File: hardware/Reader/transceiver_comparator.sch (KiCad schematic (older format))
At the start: 12 parts, among them IC7 LM339N_NOPB

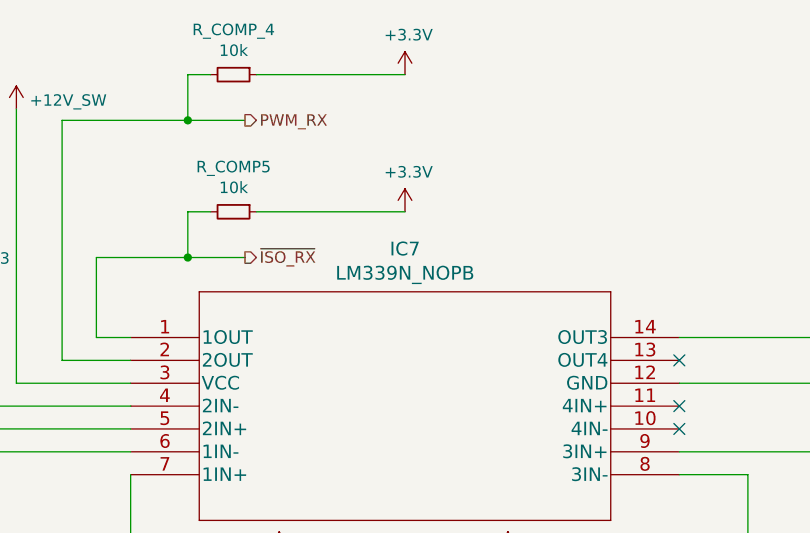
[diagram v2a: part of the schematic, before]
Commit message: Added ESD Protection. Fixed minor bugs on schematic. Attempted placement of components
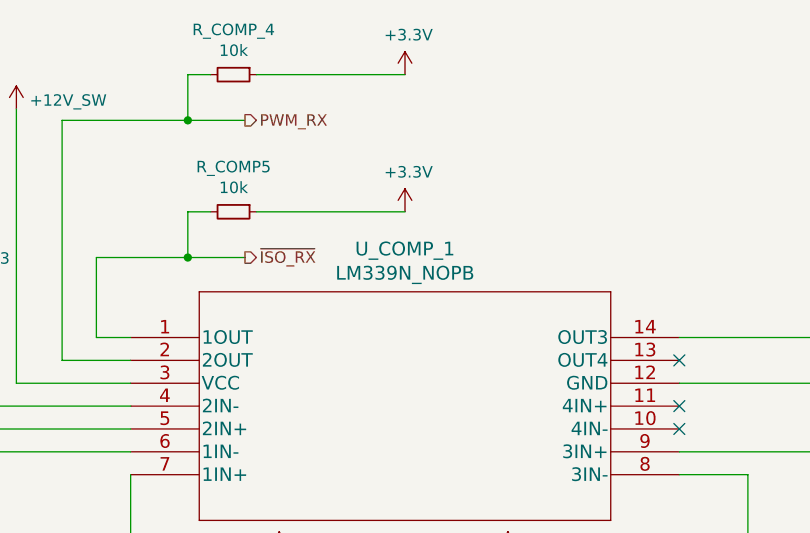
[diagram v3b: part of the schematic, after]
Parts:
- renumbered IC7 to U_COMP_1
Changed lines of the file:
@@
 $Descr USLetter 11000 8500
 encoding utf-8
-Sheet 13 18
+Sheet 8 19
 Title "CANnect Reader | Comparative Transceiver"
-Date "2020-10-20"
-Rev "0.0.01"
+Date "2020-10-25"
+Rev "0.0.03"
 Comp "CANtech"
 Comment1 "Created by Choong Jin Ng | jin8383@gmail.com"
@@
 P 4600 2200
 AR Path="/5F95F80B/5FA83833/5FB4E413" Ref="U?"  Part="1"
-AR Path="/5F95F80B/5FB4CA84/5FB4E413" Ref="IC7"  Part="1"
-F 0 "IC7" H 5800 2587 60  0000 C CNN
+AR Path="/5F95F80B/5FB4CA84/5FB4E413" Ref="U_COMP_1"  Part="1"
+F 0 "U_COMP_1" H 5800 2587 60  0000 C CNN
 F 1 "LM339N_NOPB" H 5800 2481 60  0000 C CNN
 F 2 "footprints:LM339N&slash_NOPB" H 5800 2440 60  0001 C CNN

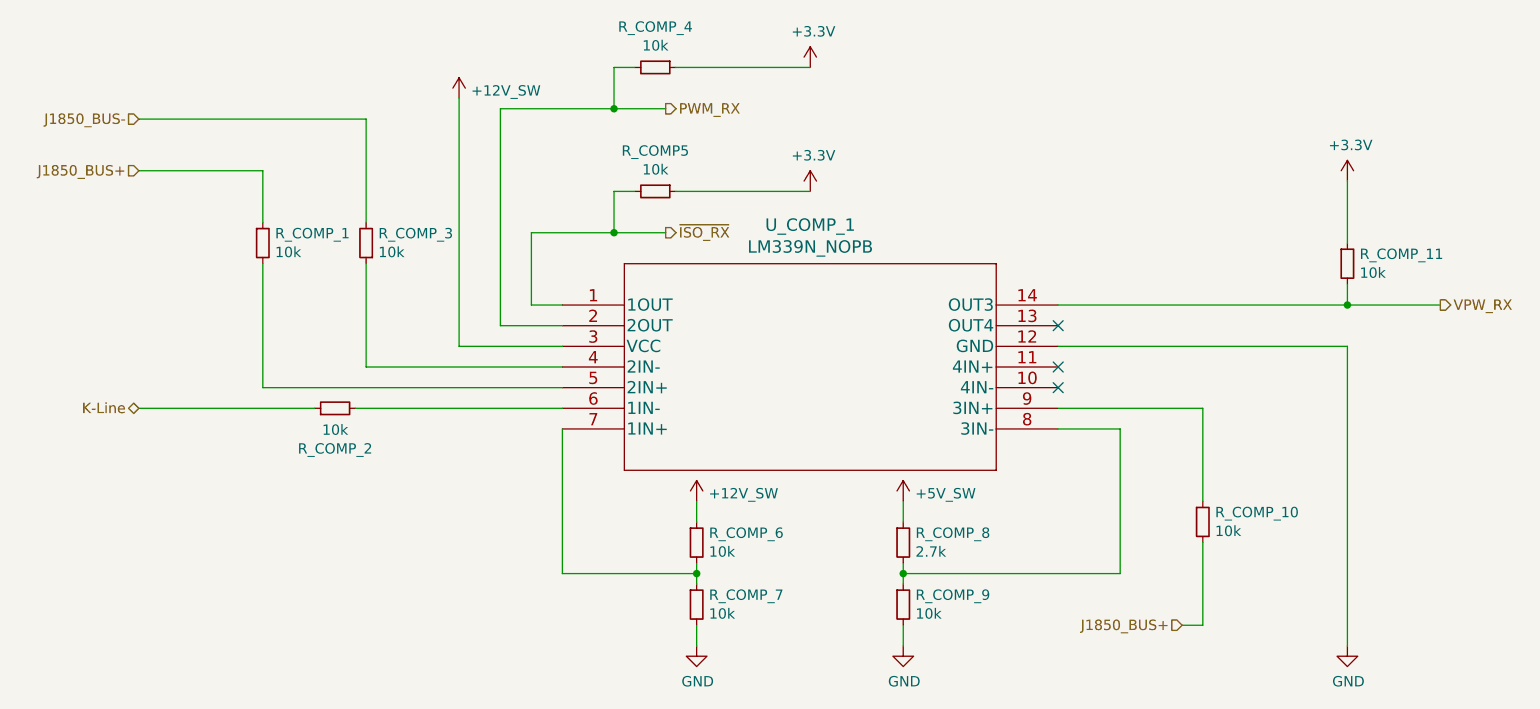
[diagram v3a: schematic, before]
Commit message: Fixed bugs on the reader schematic. Exported Schematic Electrical report
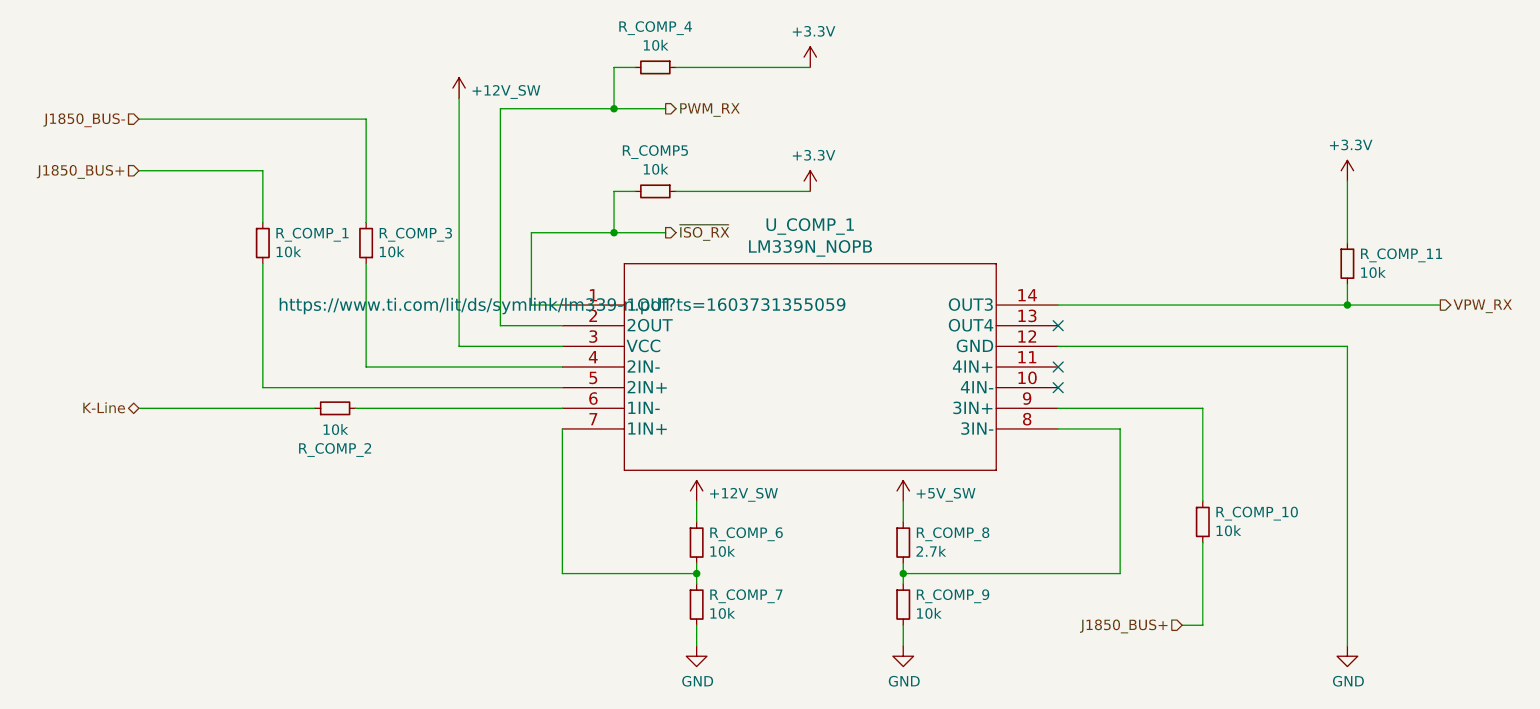
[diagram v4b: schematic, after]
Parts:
- R_COMP5, R_COMP_1, R_COMP_10, R_COMP_11, R_COMP_2, R_COMP_3, R_COMP_4, R_COMP_6, R_COMP_7, R_COMP_9: Manufacturer (none) -> Yageo; Vendor (none) -> DigiKey Canada; digikeypn (none) -> YAG2321CT-ND
- R_COMP_8: Manufacturer (none) -> Vishay Dale; Vendor (none) -> DigiKey Canada; digikeypn (none) -> 541-5328-1-ND
- U_COMP_1: Manufacturer (none) -> Texas Instruments; Part Name (none) -> LM339N_NOPB; Vendor (none) -> DigiKey Canada; digikeypn (none) -> 296-39010-5-ND
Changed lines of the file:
@@
 F 3 "https://www.yageo.com/upload/media/product/productsearch/datasheet/rchip/PYu-RT_1-to-0.01_RoHS_L_12.pdf" H 5250 3350 50  0001 C CNN
 F 4 "RT0603FRE0710KL" H 5250 3350 50  0001 C CNN "Part Name"
+F 5 "DigiKey Canada" H 5250 3350 50  0001 C CNN "Vendor"
+F 6 "YAG2321CT-ND" H 5250 3350 50  0001 C CNN "digikeypn"
+F 7 "Yageo" H 5250 3350 50  0001 C CNN "Manufacturer"
 	1    5250 3350
 	1    0    0    -1
@@
 F 3 "https://www.yageo.com/upload/media/product/productsearch/datasheet/rchip/PYu-RT_1-to-0.01_RoHS_L_12.pdf" H 5250 3650 50  0001 C CNN
 F 4 "RT0603FRE0710KL" H 5250 3650 50  0001 C CNN "Part Name"
+F 5 "DigiKey Canada" H 5250 3650 50  0001 C CNN "Vendor"
+F 6 "YAG2321CT-ND" H 5250 3650 50  0001 C CNN "digikeypn"
+F 7 "Yageo" H 5250 3650 50  0001 C CNN "Manufacturer"
 	1    5250 3650
 	1    0    0    -1
@@
 F 3 "https://www.yageo.com/upload/media/product/productsearch/datasheet/rchip/PYu-RT_1-to-0.01_RoHS_L_12.pdf" H 5050 1650 50  0001 C CNN
 F 4 "RT0603FRE0710KL" H 5050 1650 50  0001 C CNN "Part Name"
+F 5 "DigiKey Canada" H 5050 1650 50  0001 C CNN "Vendor"
+F 6 "YAG2321CT-ND" H 5050 1650 50  0001 C CNN "digikeypn"
+F 7 "Yageo" H 5050 1650 50  0001 C CNN "Manufacturer"
 	1    5050 1650
 	0    1    1    0
@@
 F 3 "https://www.yageo.com/upload/media/product/productsearch/datasheet/rchip/PYu-RT_1-to-0.01_RoHS_L_12.pdf" H 3650 1900 50  0001 C CNN
 F 4 "RT0603FRE0710KL" H 3650 1900 50  0001 C CNN "Part Name"
+F 5 "DigiKey Canada" H 3650 1900 50  0001 C CNN "Vendor"
+F 6 "YAG2321CT-ND" H 3650 1900 50  0001 C CNN "digikeypn"
+F 7 "Yageo" H 3650 1900 50  0001 C CNN "Manufacturer"
 	1    3650 1900
 	-1   0    0    1
@@
 F 3 "https://www.yageo.com/upload/media/product/productsearch/datasheet/rchip/PYu-RT_1-to-0.01_RoHS_L_12.pdf" H 3150 1900 50  0001 C CNN
 F 4 "RT0603FRE0710KL" H 3150 1900 50  0001 C CNN "Part Name"
+F 5 "DigiKey Canada" H 3150 1900 50  0001 C CNN "Vendor"
+F 6 "YAG2321CT-ND" H 3150 1900 50  0001 C CNN "digikeypn"
+F 7 "Yageo" H 3150 1900 50  0001 C CNN "Manufacturer"
 	1    3150 1900
 	1    0    0    -1
@@
 F 3 "https://www.yageo.com/upload/media/product/productsearch/datasheet/rchip/PYu-RT_1-to-0.01_RoHS_L_12.pdf" H 7700 3250 50  0001 C CNN
 F 4 "RT0603FRE0710KL" H 7700 3250 50  0001 C CNN "Part Name"
+F 5 "DigiKey Canada" H 7700 3250 50  0001 C CNN "Vendor"
+F 6 "YAG2321CT-ND" H 7700 3250 50  0001 C CNN "digikeypn"
+F 7 "Yageo" H 7700 3250 50  0001 C CNN "Manufacturer"
 	1    7700 3250
 	1    0    0    -1
@@
 F 3 "https://www.vishay.com/docs/28773/crcwce3.pdf" H 6250 3350 50  0001 C CNN
 F 4 "CRCW06032K70FKEAC" H 6250 3350 50  0001 C CNN "Part Name"
+F 5 "DigiKey Canada" H 6250 3350 50  0001 C CNN "Vendor"
+F 6 "Vishay Dale" H 6250 3350 50  0001 C CNN "Manufacturer"
+F 7 "541-5328-1-ND" H 6250 3350 50  0001 C CNN "digikeypn"
 	1    6250 3350
 	1    0    0    -1
@@
 F 3 "https://www.yageo.com/upload/media/product/productsearch/datasheet/rchip/PYu-RT_1-to-0.01_RoHS_L_12.pdf" H 6250 3650 50  0001 C CNN
 F 4 "RT0603FRE0710KL" H 6250 3650 50  0001 C CNN "Part Name"
+F 5 "DigiKey Canada" H 6250 3650 50  0001 C CNN "Vendor"
+F 6 "YAG2321CT-ND" H 6250 3650 50  0001 C CNN "digikeypn"
+F 7 "Yageo" H 6250 3650 50  0001 C CNN "Manufacturer"
 	1    6250 3650
 	1    0    0    -1
@@
 F 1 "LM339N_NOPB" H 5800 2481 60  0000 C CNN
 F 2 "footprints:LM339N&slash_NOPB" H 5800 2440 60  0001 C CNN
-F 3 "" H 4600 2200 60  0000 C CNN
+F 3 "https://www.ti.com/lit/ds/symlink/lm339-n.pdf?ts=1603731355059" H 4600 2200 60  0000 C CNN
+F 4 "LM339N_NOPB" H 4600 2200 50  0001 C CNN "Part Name"
+F 5 "Texas Instruments" H 4600 2200 50  0001 C CNN "Manufacturer"
+F 6 "DigiKey Canada" H 4600 2200 50  0001 C CNN "Vendor"
+F 7 "296-39010-5-ND" H 4600 2200 50  0001 C CNN "digikeypn"
 	1    4600 2200
 	1    0    0    -1
@@
 F 3 "https://www.yageo.com/upload/media/product/productsearch/datasheet/rchip/PYu-RT_1-to-0.01_RoHS_L_12.pdf" H 5050 1050 50  0001 C CNN
 F 4 "RT0603FRE0710KL" H 5050 1050 50  0001 C CNN "Part Name"
+F 5 "DigiKey Canada" H 5050 1050 50  0001 C CNN "Vendor"
+F 6 "YAG2321CT-ND" H 5050 1050 50  0001 C CNN "digikeypn"
+F 7 "Yageo" H 5050 1050 50  0001 C CNN "Manufacturer"
 	1    5050 1050
 	0    1    1    0
@@
 F 3 "https://www.yageo.com/upload/media/product/productsearch/datasheet/rchip/PYu-RT_1-to-0.01_RoHS_L_12.pdf" H 8400 2000 50  0001 C CNN
 F 4 "RT0603FRE0710KL" H 8400 2000 50  0001 C CNN "Part Name"
+F 5 "DigiKey Canada" H 8400 2000 50  0001 C CNN "Vendor"
+F 6 "YAG2321CT-ND" H 8400 2000 50  0001 C CNN "digikeypn"
+F 7 "Yageo" H 8400 2000 50  0001 C CNN "Manufacturer"
 	1    8400 2000
 	1    0    0    -1
@@
 F 3 "https://www.yageo.com/upload/media/product/productsearch/datasheet/rchip/PYu-RT_1-to-0.01_RoHS_L_12.pdf" H 3500 2700 50  0001 C CNN
 F 4 "RT0603FRE0710KL" H 3500 2700 50  0001 C CNN "Part Name"
+F 5 "DigiKey Canada" H 3500 2700 50  0001 C CNN "Vendor"
+F 6 "YAG2321CT-ND" H 3500 2700 50  0001 C CNN "digikeypn"
+F 7 "Yageo" H 3500 2700 50  0001 C CNN "Manufacturer"
 	1    3500 2700
 	0    -1   -1   0

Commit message: Fixed wiring issue on ESD Protection
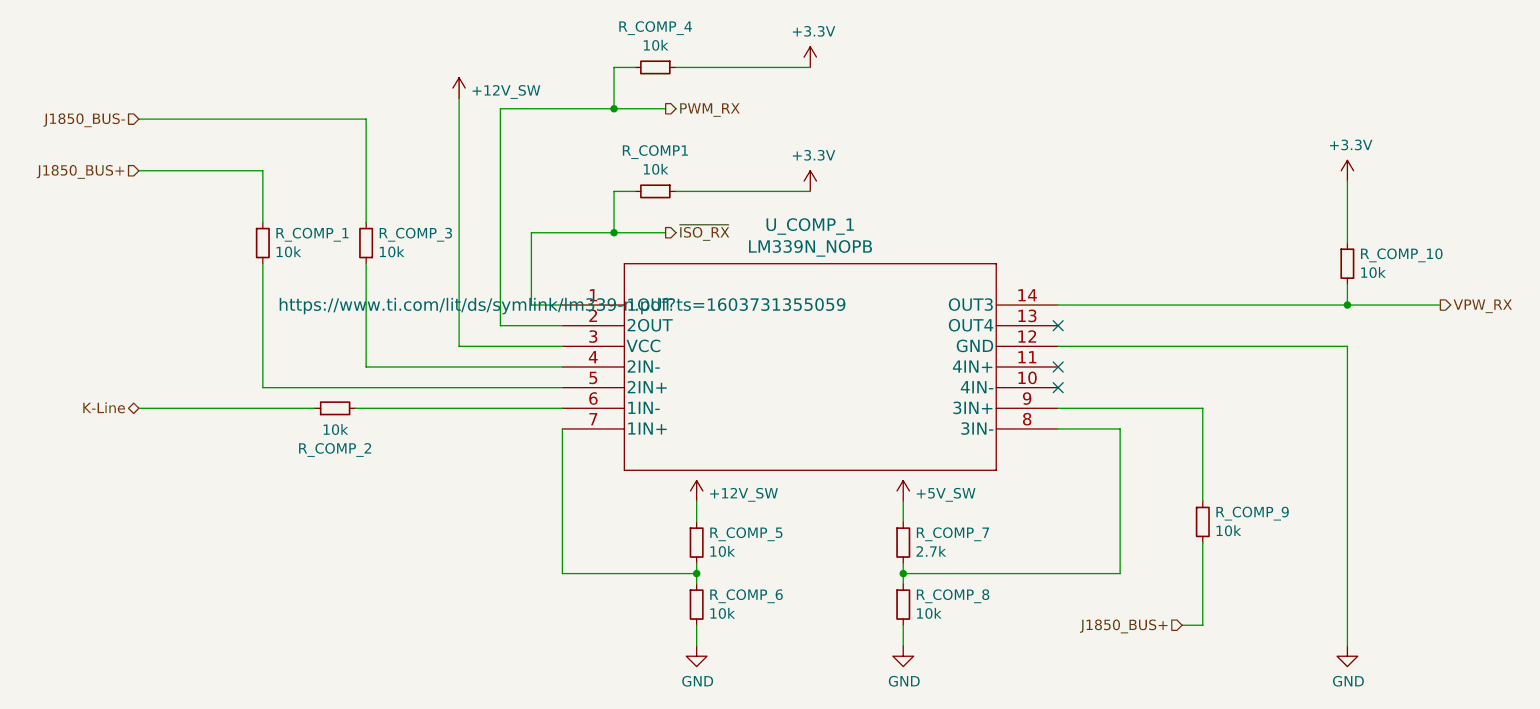
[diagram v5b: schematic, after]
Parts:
- renumbered R_COMP5 to R_COMP1, R_COMP_11 to R_COMP_10, R_COMP_6 to R_COMP_5, R_COMP_7 to R_COMP_6, R_COMP_8 to R_COMP_7, R_COMP_9 to R_COMP_8, R_COMP_10 to R_COMP_9
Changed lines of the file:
@@
 P 5250 3150
 AR Path="/5F95F80B/5FA83833/5FB4E3FC" Ref="#PWR?"  Part="1"
-AR Path="/5F95F80B/5FB4CA84/5FB4E3FC" Ref="#PWR0173"  Part="1"
-F 0 "#PWR0173" H 5250 3400 50  0001 C CNN
+AR Path="/5F95F80B/5FB4CA84/5FB4E3FC" Ref="#PWR038"  Part="1"
+F 0 "#PWR038" H 5250 3400 50  0001 C CNN
 F 1 "+12V_SW" H 5308 3187 50  0000 L CNN
 F 2 "" H 4500 3950 50  0001 C CNN
@@
 P 8400 3850
 AR Path="/5F95F80B/5FA83833/5FB4E42A" Ref="#PWR?"  Part="1"
-AR Path="/5F95F80B/5FB4CA84/5FB4E42A" Ref="#PWR0174"  Part="1"
-F 0 "#PWR0174" H 8400 3600 50  0001 C CNN
+AR Path="/5F95F80B/5FB4CA84/5FB4E42A" Ref="#PWR045"  Part="1"
+F 0 "#PWR045" H 8400 3600 50  0001 C CNN
 F 1 "GND" H 8405 3677 50  0000 C CNN
 F 2 "" H 8400 3850 50  0001 C CNN
@@
 P 5250 3850
 AR Path="/5F95F80B/5FA83833/5FB4E438" Ref="#PWR?"  Part="1"
-AR Path="/5F95F80B/5FB4CA84/5FB4E438" Ref="#PWR0175"  Part="1"
-F 0 "#PWR0175" H 5250 3600 50  0001 C CNN
+AR Path="/5F95F80B/5FB4CA84/5FB4E438" Ref="#PWR039"  Part="1"
+F 0 "#PWR039" H 5250 3600 50  0001 C CNN
 F 1 "GND" H 5255 3677 50  0000 C CNN
 F 2 "" H 5250 3850 50  0001 C CNN
@@
 P 4100 1200
 AR Path="/5F95F80B/5FA83833/5FB4E402" Ref="#PWR?"  Part="1"
-AR Path="/5F95F80B/5FB4CA84/5FB4E402" Ref="#PWR0176"  Part="1"
-F 0 "#PWR0176" H 4100 1450 50  0001 C CNN
+AR Path="/5F95F80B/5FB4CA84/5FB4E402" Ref="#PWR037"  Part="1"
+F 0 "#PWR037" H 4100 1450 50  0001 C CNN
 F 1 "+12V_SW" H 4158 1237 50  0000 L CNN
 F 2 "" H 3350 2000 50  0001 C CNN
@@
 $EndComp
 $Comp
-L Device:R_Small R?
+L Device:R_Small R_COMP_?
 U 1 1 5FB4E408
 P 5250 3350
-AR Path="/5F95F80B/5FA83833/5FB4E408" Ref="R?"  Part="1"
-AR Path="/5F95F80B/5FB4CA84/5FB4E408" Ref="R_COMP_6"  Part="1"
-F 0 "R_COMP_6" H 5309 3396 50  0000 L CNN
+AR Path="/5F95F80B/5FA83833/5FB4E408" Ref="R_COMP_?"  Part="1"
+AR Path="/5F95F80B/5FB4CA84/5FB4E408" Ref="R_COMP_5"  Part="1"
+F 0 "R_COMP_5" H 5309 3396 50  0000 L CNN
 F 1 "10k" H 5309 3305 50  0000 L CNN
 F 2 "footprints:RESC1608X55N" H 5250 3350 50  0001 C CNN
@@
 $EndComp
 $Comp
-L Device:R_Small R?
+L Device:R_Small R_COMP_?
 U 1 1 5FB4E431
 P 5250 3650
-AR Path="/5F95F80B/5FA83833/5FB4E431" Ref="R?"  Part="1"
-AR Path="/5F95F80B/5FB4CA84/5FB4E431" Ref="R_COMP_7"  Part="1"
-F 0 "R_COMP_7" H 5309 3696 50  0000 L CNN
+AR Path="/5F95F80B/5FA83833/5FB4E431" Ref="R_COMP_?"  Part="1"
+AR Path="/5F95F80B/5FB4CA84/5FB4E431" Ref="R_COMP_6"  Part="1"
+F 0 "R_COMP_6" H 5309 3696 50  0000 L CNN
 F 1 "10k" H 5309 3605 50  0000 L CNN
 F 2 "footprints:RESC1608X55N" H 5250 3650 50  0001 C CNN
@@
 $EndComp
 $Comp
-L Device:R_Small R_COMP5
+L Device:R_Small R_COMP1
 U 1 1 5FBAA6D5
 P 5050 1650
-F 0 "R_COMP5" V 4854 1650 50  0000 C CNN
+F 0 "R_COMP1" V 4854 1650 50  0000 C CNN
 F 1 "10k" V 4945 1650 50  0000 C CNN
 F 2 "footprints:RESC1608X55N" H 5050 1650 50  0001 C CNN
@@
 $EndComp
 $Comp
-L power:+3.3V #PWR0177
+L power:+3.3V #PWR041
 U 1 1 5FBAAE93
 P 5800 1650
-F 0 "#PWR0177" H 5800 1500 50  0001 C CNN
+F 0 "#PWR041" H 5800 1500 50  0001 C CNN
 F 1 "+3.3V" H 5815 1823 50  0000 C CNN
 F 2 "" H 5800 1650 50  0001 C CNN
@@
 J1850_BUS+
 $Comp
-L Device:R_Small R_COMP_10
+L Device:R_Small R_COMP_9
 U 1 1 5FBAD28A
 P 7700 3250
-F 0 "R_COMP_10" H 7759 3296 50  0000 L CNN
+F 0 "R_COMP_9" H 7759 3296 50  0000 L CNN
 F 1 "10k" H 7759 3205 50  0000 L CNN
 F 2 "footprints:RESC1608X55N" H 7700 3250 50  0001 C CNN
@@
 	7700 2700 7700 3150
 $Comp
-L Device:R_Small R_COMP_8
+L Device:R_Small R_COMP_7
 U 1 1 5FBB49DF
 P 6250 3350
-F 0 "R_COMP_8" H 6309 3396 50  0000 L CNN
+F 0 "R_COMP_7" H 6309 3396 50  0000 L CNN
 F 1 "2.7k" H 6309 3305 50  0000 L CNN
 F 2 "footprints:RESC1608X55N" H 6250 3350 50  0001 C CNN
@@
 $EndComp
 $Comp
-L Device:R_Small R_COMP_9
+L Device:R_Small R_COMP_8
 U 1 1 5FBB4DBB
 P 6250 3650
-F 0 "R_COMP_9" H 6309 3696 50  0000 L CNN
+F 0 "R_COMP_8" H 6309 3696 50  0000 L CNN
 F 1 "10k" H 6309 3605 50  0000 L CNN
 F 2 "footprints:RESC1608X55N" H 6250 3650 50  0001 C CNN
@@
 P 6250 3850
 AR Path="/5F95F80B/5FA83833/5FBB53E3" Ref="#PWR?"  Part="1"
-AR Path="/5F95F80B/5FB4CA84/5FBB53E3" Ref="#PWR0178"  Part="1"
-F 0 "#PWR0178" H 6250 3600 50  0001 C CNN
+AR Path="/5F95F80B/5FB4CA84/5FBB53E3" Ref="#PWR043"  Part="1"
+F 0 "#PWR043" H 6250 3600 50  0001 C CNN
 F 1 "GND" H 6255 3677 50  0000 C CNN
 F 2 "" H 6250 3850 50  0001 C CNN
@@
 	6250 3850 6250 3750
 $Comp
-L CANtech:+5V_SW #PWR0179
+L CANtech:+5V_SW #PWR042
 U 1 1 5FBB5CB9
 P 6250 3150
-F 0 "#PWR0179" H 6250 3400 50  0001 C CNN
+F 0 "#PWR042" H 6250 3400 50  0001 C CNN
 F 1 "+5V_SW" H 6308 3187 50  0000 L CNN
 F 2 "" H 5500 3950 50  0001 C CNN
@@
 	4100 2400 4600 2400
 $Comp
-L LM339NNOPB:LM339N_NOPB U?
+L LM339NNOPB:LM339N_NOPB U_COMP_?
 U 1 1 5FB4E413
 P 4600 2200
-AR Path="/5F95F80B/5FA83833/5FB4E413" Ref="U?"  Part="1"
+AR Path="/5F95F80B/5FA83833/5FB4E413" Ref="U_COMP_?"  Part="1"
 AR Path="/5F95F80B/5FB4CA84/5FB4E413" Ref="U_COMP_1"  Part="1"
 F 0 "U_COMP_1" H 5800 2587 60  0000 C CNN
@@
 NoConn ~ 7000 2300
 $Comp
-L Device:R_Small R_COMP_11
+L Device:R_Small R_COMP_10
 U 1 1 5FBC1B65
 P 8400 2000
-F 0 "R_COMP_11" H 8459 2046 50  0000 L CNN
+F 0 "R_COMP_10" H 8459 2046 50  0000 L CNN
 F 1 "10k" H 8459 1955 50  0000 L CNN
 F 2 "footprints:RESC1608X55N" H 8400 2000 50  0001 C CNN
@@
 VPW_RX
 $Comp
-L power:+3.3V #PWR0181
+L power:+3.3V #PWR044
 U 1 1 5FBC3E7A
 P 8400 1600
-F 0 "#PWR0181" H 8400 1450 50  0001 C CNN
+F 0 "#PWR044" H 8400 1450 50  0001 C CNN
 F 1 "+3.3V" H 8415 1773 50  0000 C CNN
 F 2 "" H 8400 1600 50  0001 C CNN
@@
 	8400 2200 8850 2200
 $Comp
-L Device:R_Small R?
+L Device:R_Small R_COMP_?
 U 1 1 5FB4E43F
 P 3500 2700
-AR Path="/5F95F80B/5FA83833/5FB4E43F" Ref="R?"  Part="1"
+AR Path="/5F95F80B/5FA83833/5FB4E43F" Ref="R_COMP_?"  Part="1"
 AR Path="/5F95F80B/5FB4CA84/5FB4E43F" Ref="R_COMP_2"  Part="1"
 F 0 "R_COMP_2" V 3304 2700 50  0000 C CNN
@@
 	5150 1650 5800 1650
 $Comp
-L power:+3.3V #PWR02
+L power:+3.3V #PWR040
 U 1 1 5FFDEA6D
 P 5800 1050
-F 0 "#PWR02" H 5800 900 50  0001 C CNN
+F 0 "#PWR040" H 5800 900 50  0001 C CNN
 F 1 "+3.3V" H 5815 1223 50  0000 C CNN
 F 2 "" H 5800 1050 50  0001 C CNN
